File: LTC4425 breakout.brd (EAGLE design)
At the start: 33 x 22.9 mm, 13 parts, among them IC1 LTC4425

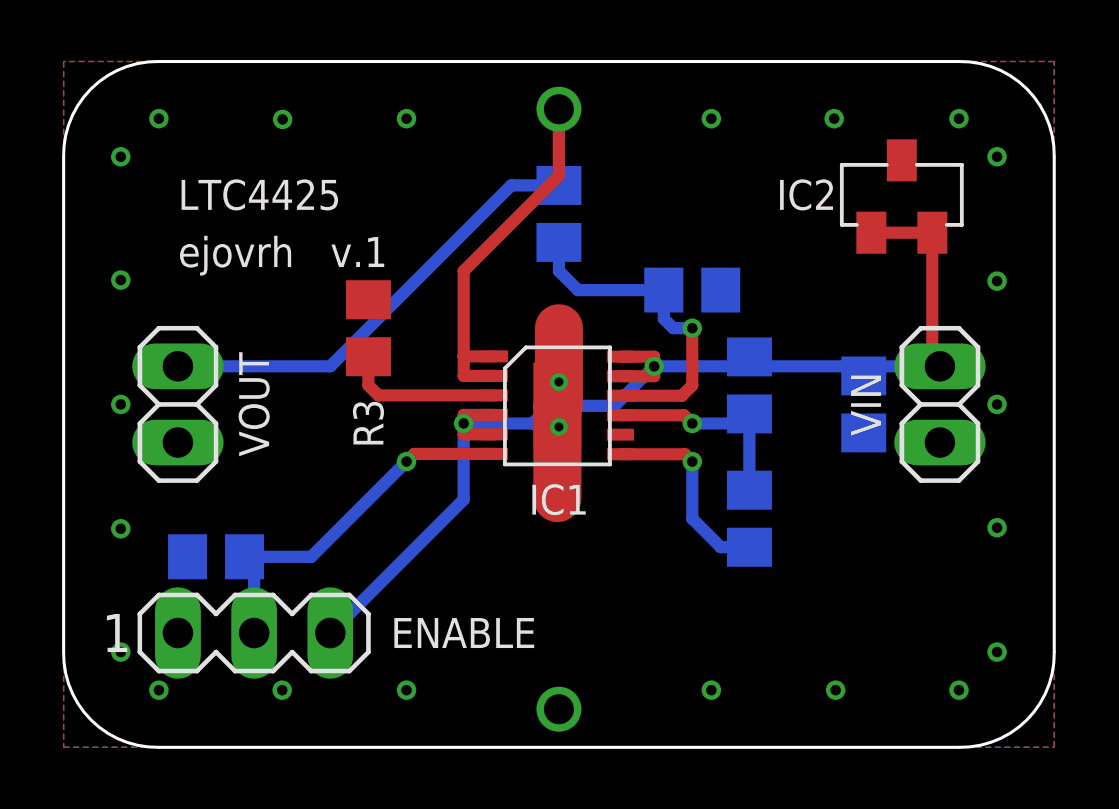
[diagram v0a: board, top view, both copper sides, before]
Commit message: - updated LTC4425 breakout: replaced the supercap, modified tplace strings
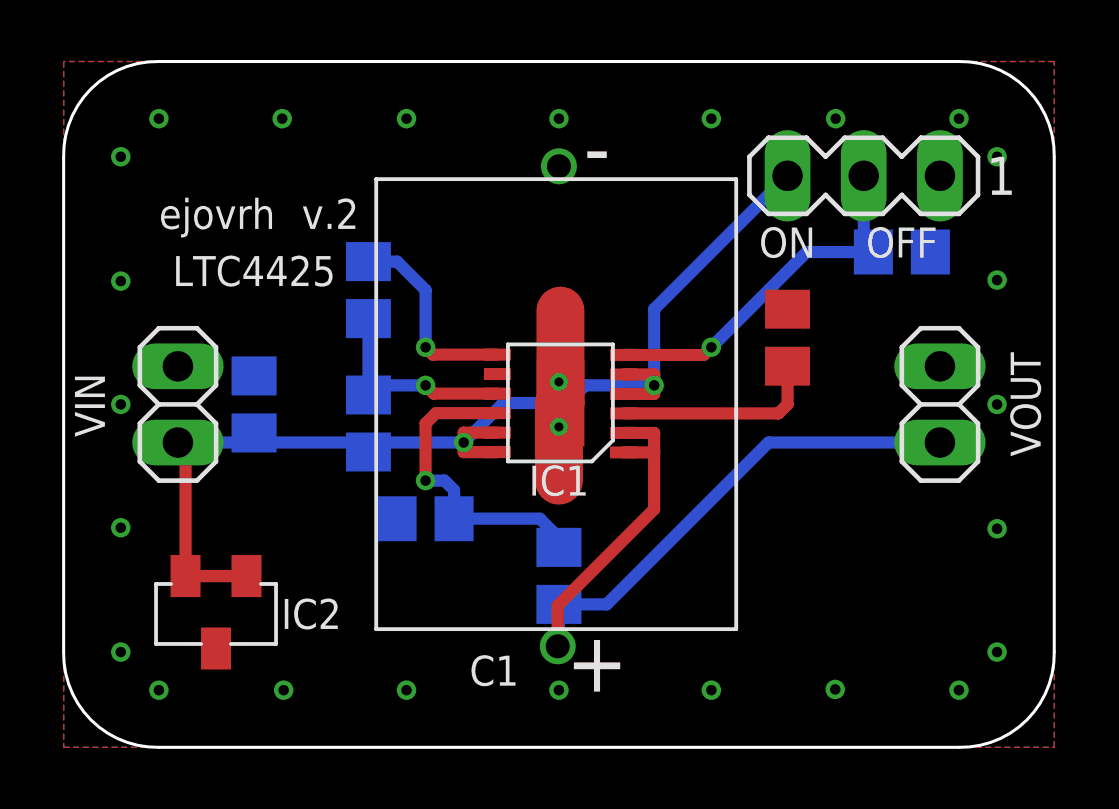
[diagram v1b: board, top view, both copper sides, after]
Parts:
- removed C3: 0.1µF, rcl:C0805
- removed ENABLE: (no value), con-lstb:MA03-1
- removed R10, R9: 470k, rcl:R0805
- added C1: MAL219691226E3, MAL219691226E3 - Supercap:TH
- added R1, R6: 10k, rcl:R0805
- added SV1: enable, con-lstb:MA03-1
- C2: value 1.5F -> 0.1µF; device EECS5R5H155 Supercap:TH -> rcl:C0805
- R2, R3: value 10k -> 150k
- R4, R5: value 150k -> 470k
- moved IC2 26.8 mm to (5.08, 4.45), turned to 180 degrees
- moved VIN 25.4 mm to (3.81, 11.4), turned to 270 degrees
- moved VOUT 25.4 mm to (29.2, 11.4), turned to 270 degrees
- moved R5 10.8 mm to (12.1, 7.62), turned to 0 degrees
- moved C2 10.2 mm to (6.35, 11.4)
- moved R4 8.98 mm to (16.5, 5.71)
- moved R2 6.75 mm to (10.2, 10.8), turned to 270 degrees
- moved R3 1.27 mm to (10.2, 15.2), flipped to the bottom
- turned IC1 to 90 degrees
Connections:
- net EN: now also R6.1, SV1.2; no longer ENABLE.2, R2.1
- net GND: now also C1.-, C2.2, R1.1, R5.2, R6.2, SV1.1; no longer C2.-, C3.2, ENABLE.1, R10.2, R2.2, R3.1
- net PFI: now also R2.1, R3.2; no longer R4.1, R5.2
- net PFI_RET: now also R3.1; no longer R5.1
- net PROG: now also R1.2; no longer R3.2
- net VIN: now also C2.1, R2.2, SV1.3; no longer C3.1, ENABLE.3, R4.2
- net VMID: now also R4.2, R5.1; no longer R10.1, R9.2
- net VOUT: now also C1.+1, R4.1; no longer C2.+, R9.1
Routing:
- net VOUT: track 30.0 -> 27.4 mm
- net PROG: track 5.29 -> 6.87 mm
- net VMID: track 11.2 -> 10.6 mm
- net GND: vias 22 -> 24
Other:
- board text added: "----"
- board text added: "1V"
- board text added: "Ichrg"
- board text added: "OFF"
- board text added: "ON"
- board text added: "Rprog"
- board text added: "Rprog = 1000 *"
- board text added: "v.2"
- board text removed: "v.1"

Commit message: - removed supercap from board and made it generic - updated gerbers and design block
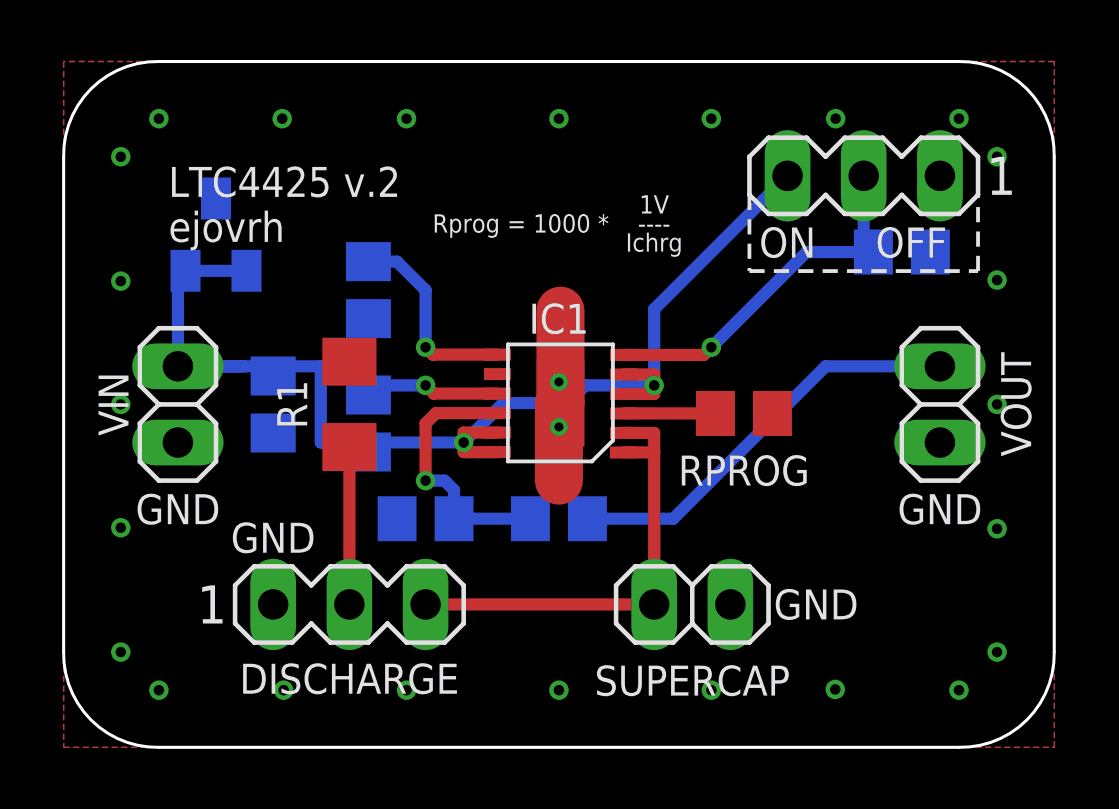
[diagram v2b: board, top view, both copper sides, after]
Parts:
- removed C1: MAL219691226E3, MAL219691226E3 - Supercap:TH
- added DISCHARGE: discharge, con-lstb:MA03-1
- added RPROG: 10k, rcl:R0805
- added SUPERCAP: SUPERCAP, pinhead:1X02
- R1: device rcl:R0805 -> rcl:R1206
- moved R1 14.8 mm to (9.53, 11.4), turned to 90 degrees
- moved IC2 12.7 mm to (5.08, 17.1), flipped to the bottom, turned to 0 degrees
- moved R4 1.91 mm to (16.5, 7.62), turned to 0 degrees
- moved C2 0.64 mm to (6.99, 11.4), turned to 270 degrees
- turned VIN to 90 degrees
- turned VOUT to 90 degrees
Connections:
- new net N$2: DISCHARGE.2, R1.1
- net GND: now also DISCHARGE.1, R1.2, RPROG.1, SUPERCAP.1; no longer C1.-, R1.1
- net PROG: now also RPROG.2; no longer R1.2
- net VOUT: now also DISCHARGE.3, SUPERCAP.2; no longer C1.+1
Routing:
- net N$2: track 0.00 -> 5.25 mm
- net VOUT: track 27.4 -> 32.6 mm
- net PROG: track 6.87 -> 3.07 mm
- net VIN: track 38.7 -> 41.8 mm
- net VMID: track 10.6 -> 9.34 mm
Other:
- board text added: "GND"
- board text added: "LTC4425 v.2 ejovrh"
- board text removed: "LTC4425"
- board text removed: "ejovrh"
- board text removed: "v.2"

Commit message: - finalized LTC4425 breakout.brd, written BOM and created gerbers
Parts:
- IC2: value (none) -> PESD5V2S2UT
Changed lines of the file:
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@@
 <?xml version="1.0" encoding="utf-8"?>
 <!DOCTYPE eagle SYSTEM "eagle.dtd">
-<eagle version="8.6.1">
+<eagle version="9.0.0">
 <drawing>
 <settings>
@@
 <layer number="14" name="Route14" color="1" fill="6" visible="no" active="no"/>
 <layer number="15" name="Route15" color="4" fill="6" visible="no" active="no"/>
-<layer number="16" name="Bottom" color="1" fill="1" visible="no" active="yes"/>
+<layer number="16" name="Bottom" color="1" fill="1" visible="yes" active="yes"/>
 <layer number="17" name="Pads" color="2" fill="1" visible="yes" active="yes"/>
 <layer number="18" name="Vias" color="2" fill="1" visible="yes" active="yes"/>
@@
 <layer number="20" name="Dimension" color="24" fill="1" visible="yes" active="yes"/>
 <layer number="21" name="tPlace" color="7" fill="1" visible="yes" active="yes"/>
-<layer number="22" name="bPlace" color="7" fill="1" visible="no" active="yes"/>
+<layer number="22" name="bPlace" color="7" fill="1" visible="yes" active="yes"/>
 <layer number="23" name="tOrigins" color="15" fill="1" visible="yes" active="yes"/>
-<layer number="24" name="bOrigins" color="15" fill="1" visible="no" active="yes"/>
+<layer number="24" name="bOrigins" color="15" fill="1" visible="yes" active="yes"/>
 <layer number="25" name="tNames" color="7" fill="1" visible="yes" active="yes"/>
-<layer number="26" name="bNames" color="7" fill="1" visible="no" active="yes"/>
+<layer number="26" name="bNames" color="7" fill="1" visible="yes" active="yes"/>
 <layer number="27" name="tValues" color="7" fill="1" visible="no" active="yes"/>
 <layer number="28" name="bValues" color="7" fill="1" visible="no" active="yes"/>
@@
 <layer number="38" name="bTest" color="7" fill="1" visible="no" active="yes"/>
 <layer number="39" name="tKeepout" color="4" fill="11" visible="yes" active="yes"/>
-<layer number="40" name="bKeepout" color="1" fill="11" visible="no" active="yes"/>
+<layer number="40" name="bKeepout" color="1" fill="11" visible="yes" active="yes"/>
 <layer number="41" name="tRestrict" color="4" fill="10" visible="yes" active="yes"/>
-<layer number="42" name="bRestrict" color="1" fill="10" visible="no" active="yes"/>
+<layer number="42" name="bRestrict" color="1" fill="10" visible="yes" active="yes"/>
 <layer number="43" name="vRestrict" color="2" fill="10" visible="no" active="yes"/>
-<layer number="44" name="Drills" color="7" fill="1" visible="yes" active="yes"/>
+<layer number="44" name="Drills" color="7" fill="1" visible="no" active="yes"/>
 <layer number="45" name="Holes" color="7" fill="1" visible="yes" active="yes"/>
 <layer number="46" name="Milling" color="3" fill="1" visible="yes" active="yes"/>
 <layer number="47" name="Measures" color="7" fill="1" visible="no" active="yes"/>
-<layer number="48" name="Document" color="7" fill="1" visible="yes" active="yes"/>
+<layer number="48" name="Document" color="7" fill="1" visible="no" active="yes"/>
 <layer number="49" name="Reference" color="7" fill="1" visible="no" active="yes"/>
 <layer number="50" name="dxf" color="7" fill="1" visible="no" active="no"/>
 <layer number="51" name="tDocu" color="7" fill="1" visible="yes" active="yes"/>
-<layer number="52" name="bDocu" color="7" fill="1" visible="no" active="yes"/>
+<layer number="52" name="bDocu" color="7" fill="1" visible="yes" active="yes"/>
 <layer number="53" name="tGND_GNDA" color="7" fill="9" visible="no" active="no"/>
 <layer number="54" name="bGND_GNDA" color="1" fill="9" visible="no" active="no"/>
@@
 <attribute name="VALUE" x="32.385" y="8.89" size="1.27" layer="27" rot="R90"/>
 </element>
-<element name="IC2" library="PESDxS2UT" package="SOT-23" value="" x="5.08" y="17.145" smashed="yes" rot="MR0">
+<element name="IC2" library="PESDxS2UT" package="SOT-23" value="PESD5V2S2UT" x="5.08" y="17.145" smashed="yes" rot="MR0">
 <attribute name="NAME" x="8.255" y="17.145" size="1" layer="22" font="vector" rot="MR0" align="center"/>
-<attribute name="VALUE" x="5.08" y="13.645" size="1.27" layer="22" font="vector" rot="MR0" align="center"/>
 </element>
 <element name="SV1" library="con-lstb" library_urn="urn:adsk.eagle:library:162" package="MA03-1" package3d_urn="urn:adsk.eagle:package:8339/1" value="enable" x="26.67" y="19.05" smashed="yes" rot="R180">

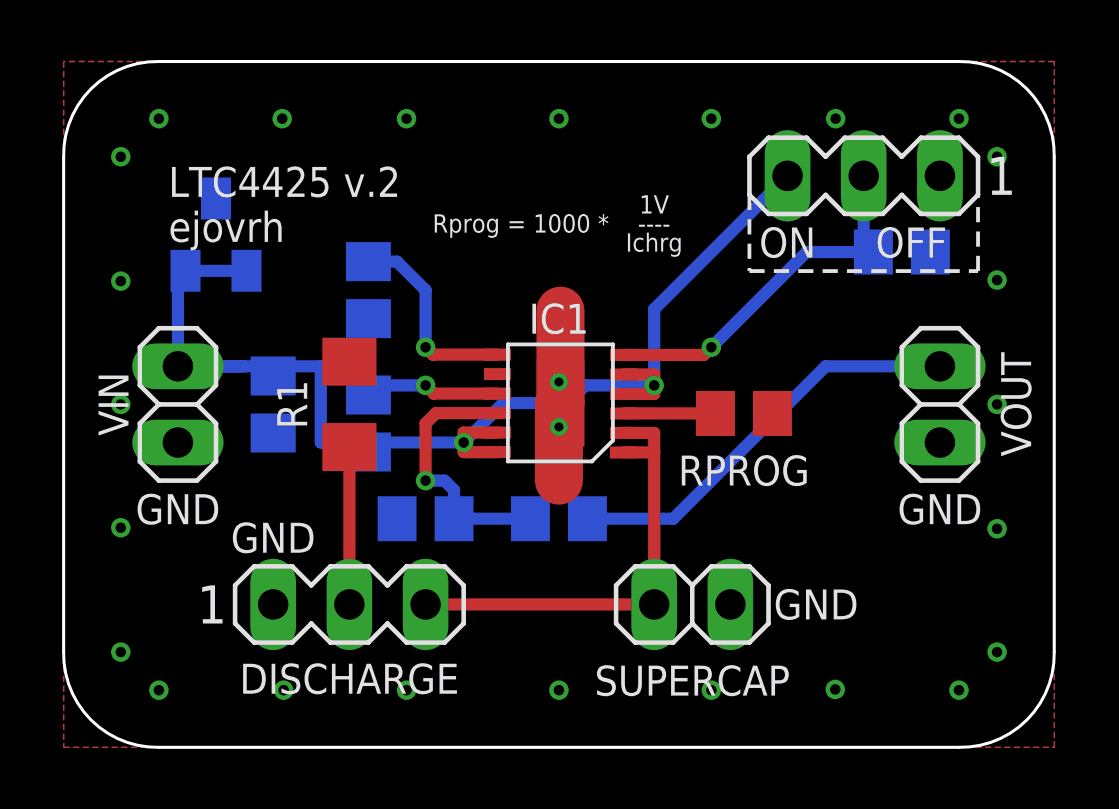
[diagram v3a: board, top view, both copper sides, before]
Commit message: - updated LTC4425 breakout with 0402 SMD passives, updated BOM and gerbers
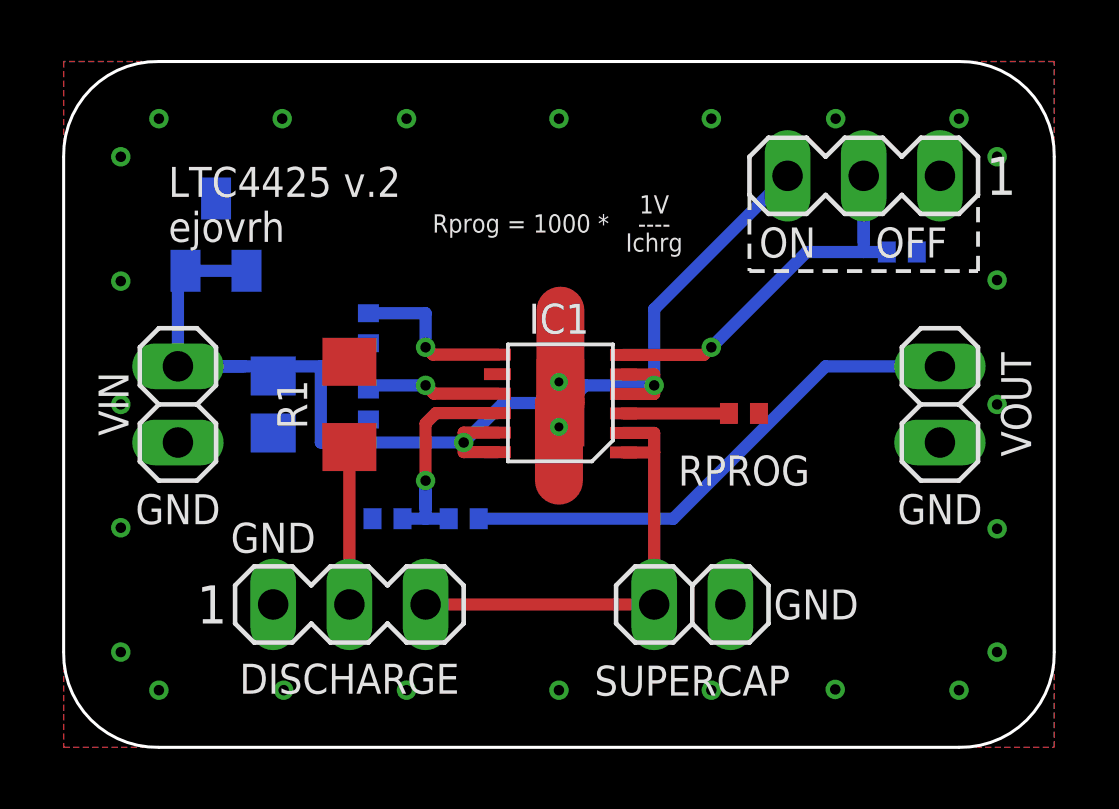
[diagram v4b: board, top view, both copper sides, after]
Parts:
- R2, R3, R4, R5, R6, RPROG: device rcl:R0805 -> rcl:R0402
- moved R4 3.18 mm to (13.3, 7.62)
- moved R3 1.27 mm to (10.2, 14.0)
- moved R5 1.27 mm to (10.8, 7.62)
- moved R2 0.63 mm to (10.2, 11.4)
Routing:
- net VOUT: track 32.6 -> 35.7 mm
- net EN: track 12.4 -> 15.0 mm
- net PFI_RET: track 6.70 -> 5.54 mm
- net VMID: track 9.34 -> 8.20 mm
- net PFI: track 7.09 -> 6.09 mm

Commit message: dummy test code for an arduino uno and the breakout board
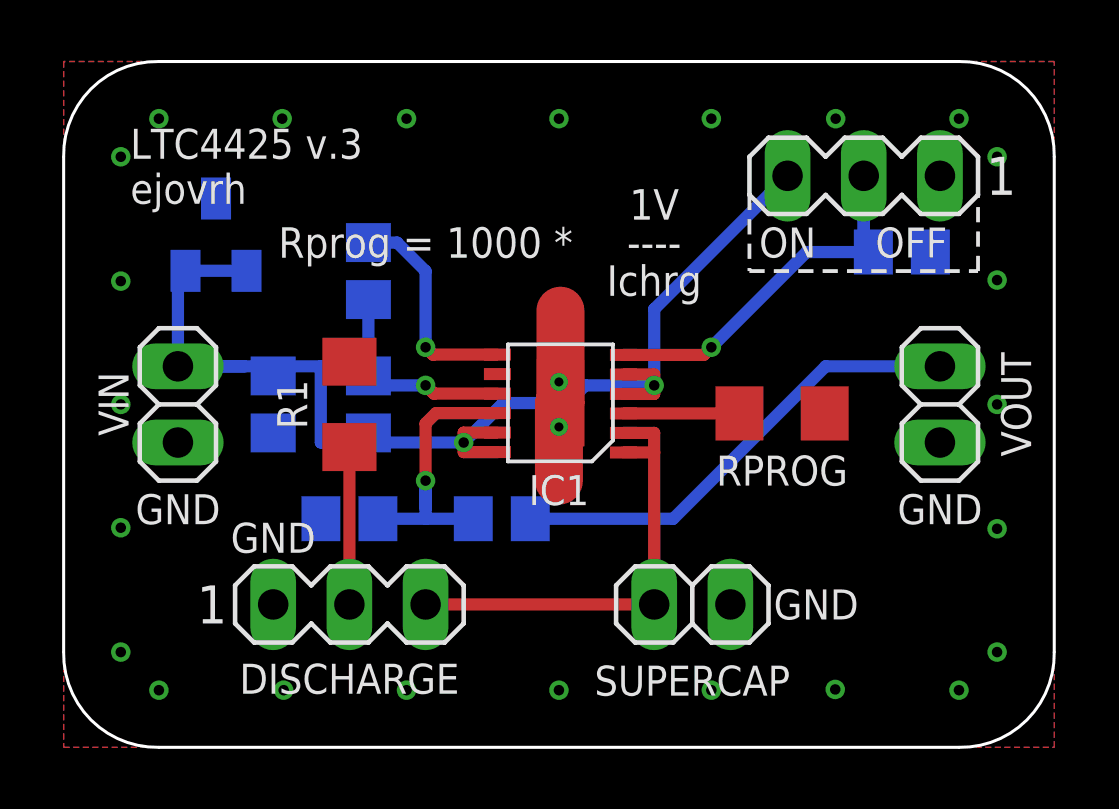
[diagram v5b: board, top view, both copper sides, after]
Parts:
- R2, R3, R4, R5, R6: device rcl:R0402 -> rcl:R0805
- RPROG: device rcl:R0402 -> rcl:R1206
- moved R3 1.90 mm to (10.2, 15.9)
- moved RPROG 1.27 mm to (23.9, 11.1)
- moved R4 1.27 mm to (14.6, 7.62)
- moved R5 1.27 mm to (9.53, 7.62)
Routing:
- net PFI_RET: track 5.54 -> 7.33 mm
- net VOUT: track 35.7 -> 34.0 mm
- net VMID: track 8.20 -> 9.84 mm
- net PFI: track 6.09 -> 7.27 mm
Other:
- board text added: "LTC4425 v.3 ejovrh"
- board text removed: "LTC4425 v.2 ejovrh"
